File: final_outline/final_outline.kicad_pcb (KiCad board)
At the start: 2 copper layers, 99.5 x 75 mm, 31 parts, among them P001 CANCONNECTOR, P002 CONN_01X14, P100 ISP, P101 DEBUG_LED, U401 MCP2551-I/SN, U403 LPC11C14, U501 MCP1755-33, U502 MCP1755-5, U503 Zsr1000gta

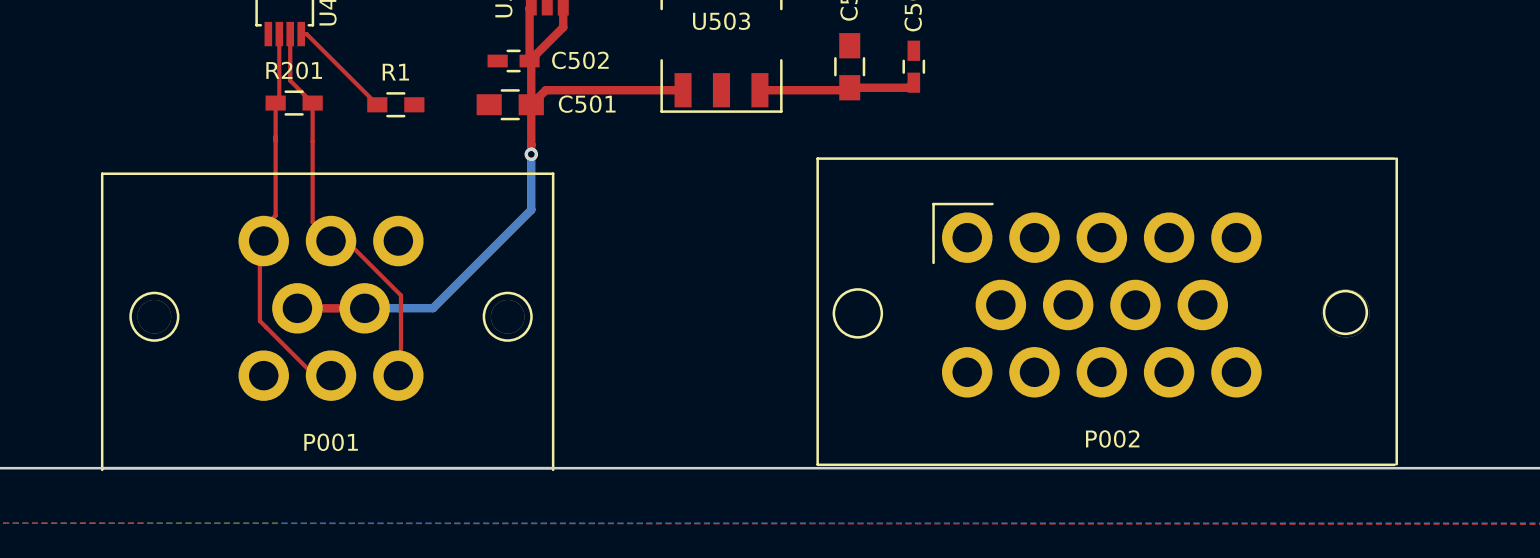
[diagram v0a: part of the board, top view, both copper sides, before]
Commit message: fixed board spacing
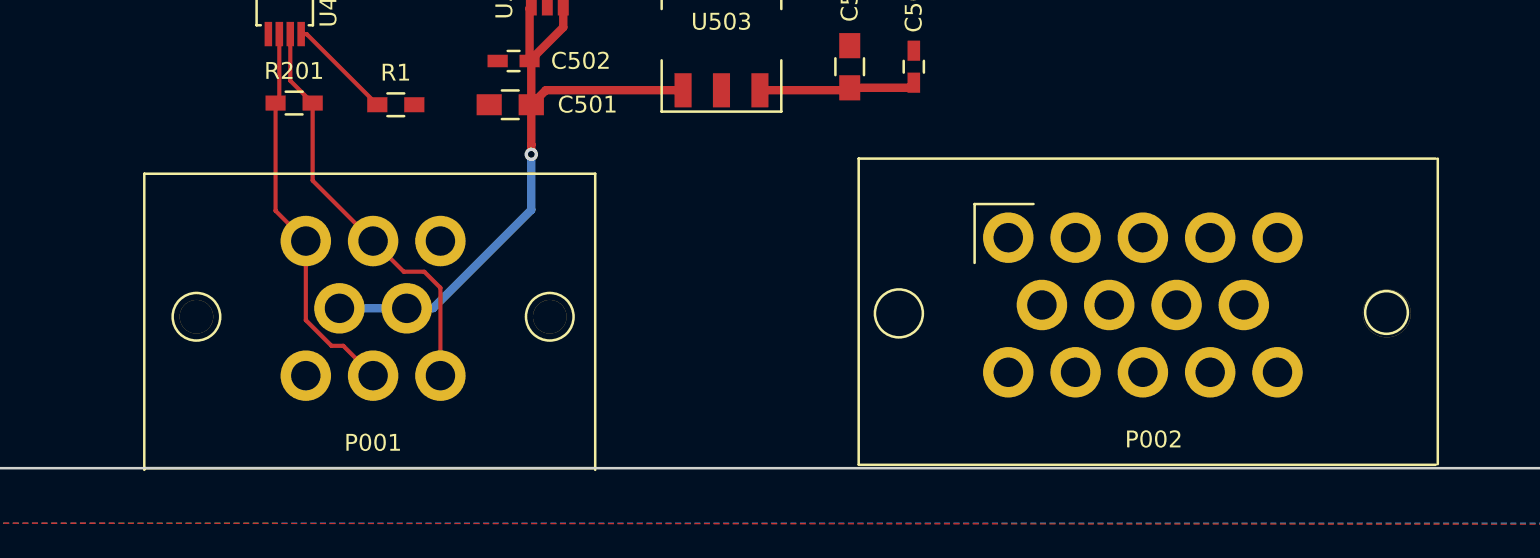
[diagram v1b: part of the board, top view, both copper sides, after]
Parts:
- moved P001 2.50 mm to (123.2, 122.5)
- moved P002 2.44 mm to (165.0, 114.3)
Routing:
- net +12V: track 42.1 -> 38.1 mm
- net /BACK_PANEL/CANH: track 23.2 -> 24.3 mm
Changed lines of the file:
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@@
-(kicad_pcb (version 4) (host pcbnew 4.0.0-rc1-stable)
+(kicad_pcb (version 4) (host pcbnew 4.0.1-stable)
   (general
     (links 81)
-    (no_connects 0)
-    (area 102.424999 52.924999 202.075001 128.075001)
+    (no_connects 4)
+    (area 102.424999 49.875 215 136.899792)
     (thickness 1.6)
     (drawings 6)
-    (tracks 308)
+    (tracks 300)
     (zones 0)
     (modules 31)
@@
   )
   (module MITEVT_AUTOMOTIVECON:776280-1 locked (layer F.Cu)
-    (at 120.75 122.5)
+    (at 123.25 122.5)
     (fp_text reference P001 (at 4 4) (layer F.SilkS)
       (effects (font (size 1 1) (thickness 0.15)))
@@
   )
   (module MITEVT_AUTOMOTIVECON:776267-1 (layer F.Cu)
-    (at 162.56 114.3)
+    (at 165 114.3)
     (fp_text reference P002 (at 8.65 12) (layer F.SilkS)
       (effects (font (size 1 1) (thickness 0.15)))
@@
   (segment (start 128.27 82.99) (end 129.17 82.99) (width 0.25) (layer F.Cu) (net 16))
   (segment (start 133.78 82.79) (end 134.08 82.49) (width 0.5) (layer F.Cu) (net 16))
+  (segment (start 130.295001 116.325001) (end 131.25 117.28) (width 0.25) (layer F.Cu) (net 17))
+  (segment (start 131.25 117.28) (end 131.25 122.5) (width 0.25) (layer F.Cu) (net 17))
+  (segment (start 127.25 114.5) (end 129.075001 116.325001) (width 0.25) (layer F.Cu) (net 17))
+  (segment (start 129.075001 116.325001) (end 130.295001 116.325001) (width 0.25) (layer F.Cu) (net 17))
+  (segment (start 123.655 106.72441) (end 123.655 110.905) (width 0.25) (layer F.Cu) (net 17))
+  (segment (start 123.655 110.905) (end 127.25 114.5) (width 0.25) (layer F.Cu) (net 17))
   (segment (start 122.325 102.2) (end 122.325 104.969) (width 0.25) (layer F.Cu) (net 17))
   (segment (start 122.325 104.969) (end 123.655 106.299) (width 0.25) (layer F.Cu) (net 17))
-  (segment (start 123.655 108.585) (end 123.655 106.72441) (width 0.25) (layer F.Cu) (net 17))
-  (segment (start 124.75 114.463) (end 123.655 113.368) (width 0.25) (layer F.Cu) (net 17))
-  (segment (start 123.655 113.368) (end 123.655 108.585) (width 0.25) (layer F.Cu) (net 17) (status 20))
-  (segment (start 124.75 114.5) (end 124.75 114.463) (width 0.25) (layer F.Cu) (net 17))
-  (segment (start 124.75 114.5) (end 125.676 114.5) (width 0.25) (layer F.Cu) (net 17))
-  (segment (start 125.676 114.5) (end 128.905 117.729) (width 0.25) (layer F.Cu) (net 17))
-  (segment (start 128.905 117.729) (end 128.905 122.345) (width 0.25) (layer F.Cu) (net 17))
-  (segment (start 128.905 122.345) (end 128.75 122.5) (width 0.25) (layer F.Cu) (net 17))
   (segment (start 157.353 67.31) (end 180.82 67.31) (width 0.25) (layer F.Cu) (net 18))
   (segment (start 180.82 67.31) (end 182.88 65.25) (width 0.25) (layer F.Cu) (net 18))
@@
   (segment (start 119.6 92.25) (end 119.75 92.4) (width 0.5) (layer F.Cu) (net 64))
   (segment (start 119.6 90.6) (end 119.55 90.65) (width 0.5) (layer F.Cu) (net 64))
+  (segment (start 123.25 114.5) (end 123.25 119.201002) (width 0.25) (layer F.Cu) (net 65))
+  (segment (start 123.25 119.201002) (end 124.774998 120.726) (width 0.25) (layer F.Cu) (net 65))
+  (segment (start 125.476 120.726) (end 124.774998 120.726) (width 0.25) (layer F.Cu) (net 65))
+  (segment (start 127.25 122.5) (end 125.476 120.726) (width 0.25) (layer F.Cu) (net 65))
+  (segment (start 121.455 106.299) (end 121.455 112.705) (width 0.25) (layer F.Cu) (net 65))
+  (segment (start 121.455 112.705) (end 123.25 114.5) (width 0.25) (layer F.Cu) (net 65))
   (segment (start 121.675 102.2) (end 121.675 106.079) (width 0.25) (layer F.Cu) (net 65))
   (segment (start 121.675 106.079) (end 121.455 106.299) (width 0.25) (layer F.Cu) (net 65))
-  (segment (start 121.455 108.458) (end 121.455 106.299) (width 0.25) (layer F.Cu) (net 65))
-  (segment (start 121.455 108.585) (end 121.455 108.458) (width 0.25) (layer F.Cu) (net 65))
-  (segment (start 121.455 108.458) (end 121.455 108.288) (width 0.25) (layer F.Cu) (net 65))
-  (segment (start 120.75 113.692) (end 121.455 112.987) (width 0.25) (layer F.Cu) (net 65))
-  (segment (start 121.455 112.987) (end 121.455 108.585) (width 0.25) (layer F.Cu) (net 65) (status 20))
-  (segment (start 120.75 114.5) (end 120.75 113.692) (width 0.25) (layer F.Cu) (net 65))
-  (segment (start 124.75 122.5) (end 123.77 122.5) (width 0.25) (layer F.Cu) (net 65))
-  (segment (start 123.77 122.5) (end 120.904 119.634) (width 0.25) (layer F.Cu) (net 65))
-  (segment (start 120.904 119.634) (end 120.523 119.253) (width 0.25) (layer F.Cu) (net 65))
-  (segment (start 120.523 119.253) (end 120.523 114.727) (width 0.25) (layer F.Cu) (net 65))
-  (segment (start 120.523 114.727) (end 120.75 114.5) (width 0.25) (layer F.Cu) (net 65))
   (segment (start 115.210295 86.210295) (end 114.989705 86.210295) (width 0.25) (layer F.Cu) (net 66))
   (segment (start 112.4 92.6) (end 115.4 95.6) (width 0.25) (layer F.Cu) (net 66))
@@
   (segment (start 130.81 118.491) (end 136.652 112.649) (width 0.5) (layer B.Cu) (net 69))
   (segment (start 136.652 109.347) (end 136.652 108.781315) (width 0.5) (layer F.Cu) (net 69))
-  (segment (start 122.75 118.5) (end 126.75 118.5) (width 0.5) (layer F.Cu) (net 69))
   (segment (start 122.975 102.2) (end 123.3 102.2) (width 0.25) (layer F.Cu) (net 71))
   (segment (start 123.3 102.2) (end 127.5 106.4) (width 0.25) (layer F.Cu) (net 71))
